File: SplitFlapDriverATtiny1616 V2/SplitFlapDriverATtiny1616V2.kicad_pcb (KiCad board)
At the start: 2 copper layers, 30 x 60 mm, 17 parts, among them J1 UPDI Programming, J2 BUS POGO, J3 Stepper Connector, J4 Hall Effect, J5 Conn_01x06_Pin, U1 ATtiny1616-MNR, U2 ULN2003ADR, U3 SN65HVD72DR, U5 SPX3819M5-L-3-3

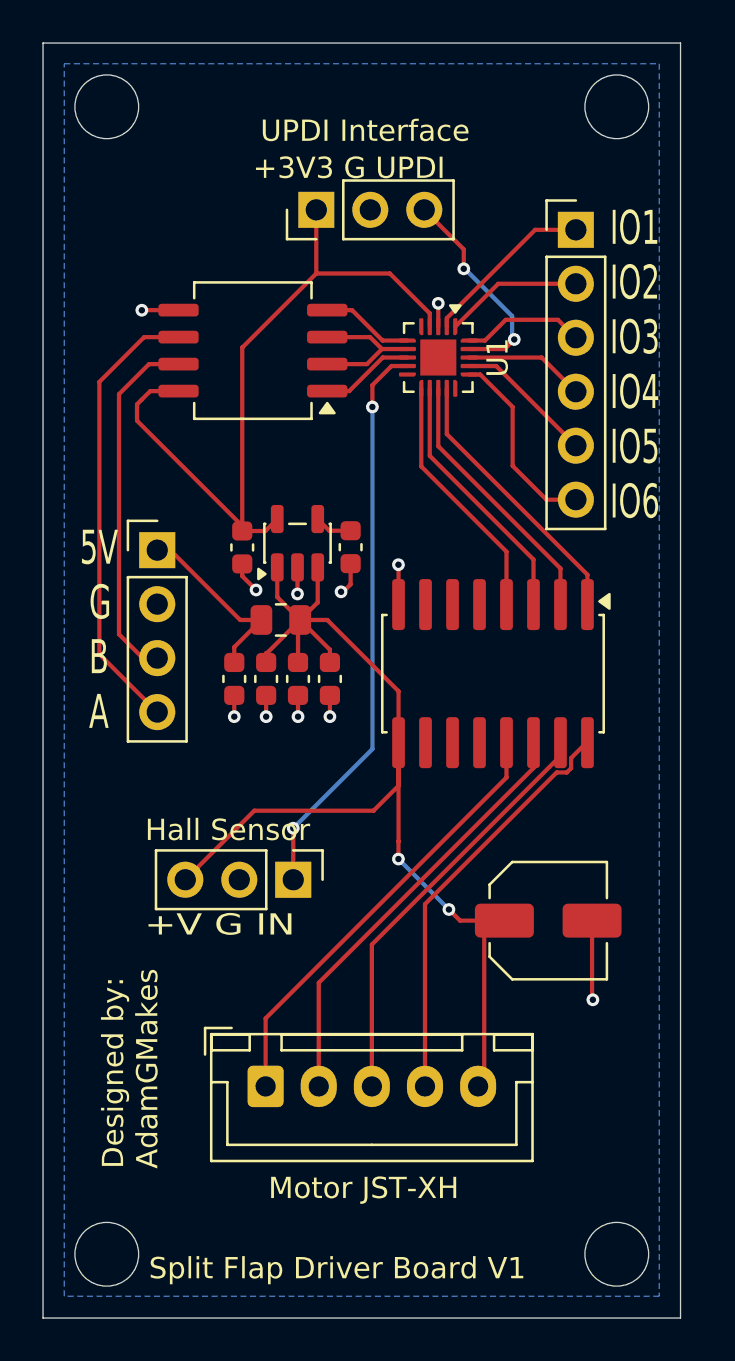
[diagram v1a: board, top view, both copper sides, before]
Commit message: Version 2 of Hub and Module Board
Finished and ordered bus board and V2 or Module board (50x)
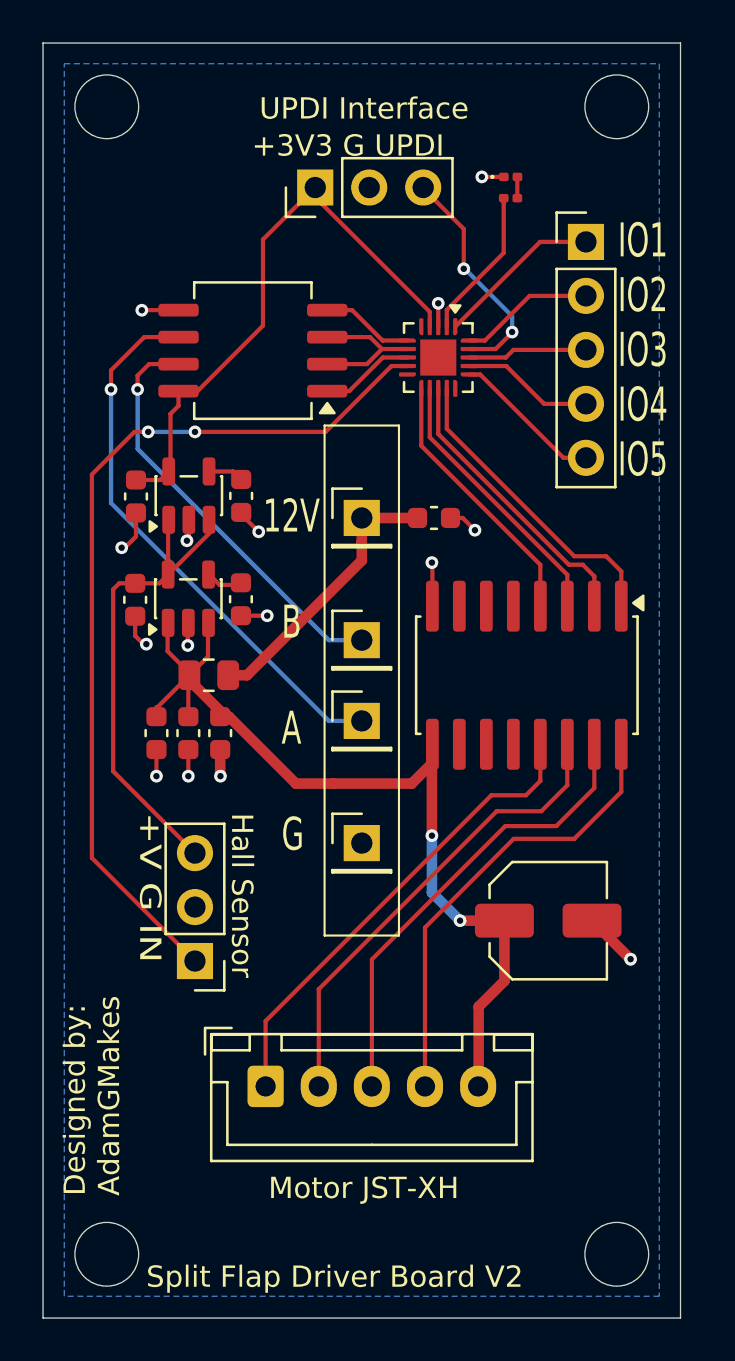
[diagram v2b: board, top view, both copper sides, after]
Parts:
- added C8: 470n, Capacitor_SMD:C_0603_1608Metric, F.Cu at (129.3, 106.2)
- added C9: 10u, Capacitor_SMD:C_0603_1608Metric, F.Cu at (124.3, 106.2)
- added D1: LED, LED_SMD:LED_0201_0603Metric, F.Cu at (142.0, 86.3)
- added J6: Conn_01x01_Pin, Connector_PinHeader_2.54mm:PinHeader_1x01_P2.54mm_Vertical, F.Cu at (135.0, 117.7)
- added J7: Conn_01x01_Pin, Connector_PinHeader_2.54mm:PinHeader_1x01_P2.54mm_Vertical, F.Cu at (135.0, 108.1)
- added J8: Conn_01x01_Pin, Connector_PinHeader_2.54mm:PinHeader_1x01_P2.54mm_Vertical, F.Cu at (135.0, 111.9)
- added R2: 60R, Resistor_SMD:R_0201_0603Metric, F.Cu at (142.0, 87.3)
- added U6: SPX3819M5-L-5-0, Package_TO_SOT_SMD:SOT-23-5, F.Cu at (126.8, 106.2)
- J2: value BUS POGO -> Conn_01x01_Pin; footprint Connector_PinHeader_2.54mm:PinHeader_1x04_P2.54mm_Vertical -> Connector_PinHeader_2.54mm:PinHeader_1x01_P2.54mm_Vertical
- J5: value Conn_01x06_Pin -> Conn_01x05_Pin; footprint Connector_PinHeader_2.54mm:PinHeader_1x06_P2.54mm_Vertical -> Connector_PinHeader_2.54mm:PinHeader_1x05_P2.54mm_Vertical
- moved C2 12.1 mm to (138.4, 102.3), turned to 0 degrees
- moved J2 9.74 mm to (135.0, 102.3)
- moved J4 6.00 mm to (127.2, 123.2), turned to 180 degrees
- moved C3 5.76 mm to (125.3, 112.5)
- moved C4 5.76 mm to (126.8, 112.5)
- moved C7 5.76 mm to (128.3, 112.5)
- moved C6 5.69 mm to (129.3, 101.3)
- moved U5 5.58 mm to (126.9, 101.3)
- moved C5 5.55 mm to (124.4, 101.3)
- moved R1 4.27 mm to (127.8, 109.8), turned to 180 degrees
- moved U2 1.59 mm to (142.8, 109.8)
- moved J1 1.05 mm to (132.8, 86.8)
- moved J5 0.74 mm to (145.6, 89.4)
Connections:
- J4 pad 3: +VBUSF -> +5V
- U1 pad 1: IO2 -> IO1
- U1 pad 16: IO6 -> IO5
- U1 pad 17: IO5 -> IO4
- U1 pad 18: IO4 -> IO3
- U1 pad 2: IO1 -> STATUS_LED
- U1 pad 20: IO3 -> IO2
- U5 pad 1: +VBUSF -> +5V
- U5 pad 3: +VBUSF -> +5V
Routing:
- net +5V: track 0.00 -> 22.9 mm
- net HALL_IN: track 26.8 -> 42.0 mm
- net +VBUSF: track 56.1 -> 45.4 mm
- net IO6: track 9.09 -> 0.00 mm
- net +3V3: track 35.4 -> 27.2 mm
- net STATUS_LED: track 0.00 -> 7.39 mm
- net GND: track 16.8 -> 23.0 mm, vias 11 -> 15
- net RS465_A: track 21.3 -> 26.1 mm, vias 0 -> 1
- net +VBUS: track 8.80 -> 13.3 mm
- net RS465_B: track 17.0 -> 19.9 mm, vias 0 -> 1
- net M3: track 20.4 -> 22.7 mm
- net M2: track 19.9 -> 21.8 mm
- net M1: track 19.6 -> 21.6 mm
- net Net-(U6-BP): track 0.00 -> 1.78 mm
- net ULN_IN1: track 12.9 -> 14.5 mm
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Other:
- board text added: "12V B A G"
- board text added: "IO1 IO2 IO3 IO4 IO5"
- board text added: "Split Flap Driver Board V2"
- board text removed: "5V G B A"
- board text removed: "IO1 IO2 IO3 IO4 IO5 IO6"
- board text removed: "Split Flap Driver Board V1"
